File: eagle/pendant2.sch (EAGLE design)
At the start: 7 parts, among them U1 ATTINY85-20PU

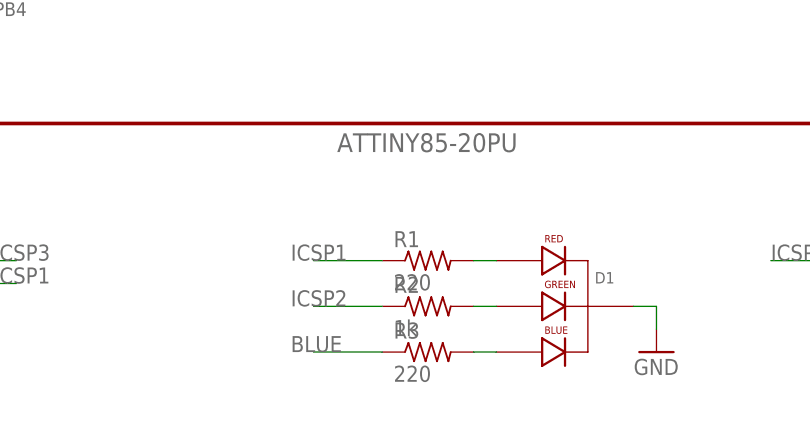
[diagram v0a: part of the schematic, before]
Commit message: Made the board yet smaller
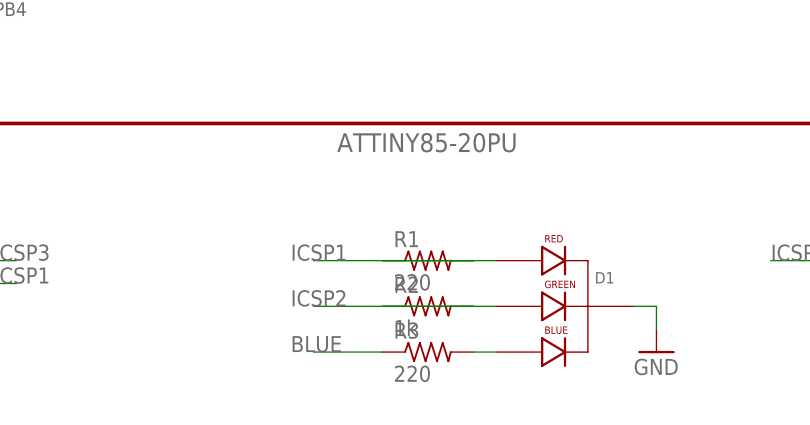
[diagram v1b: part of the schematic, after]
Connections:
- net ICSP1: now also R1.2; no longer R1.1
- net ICSP2: now also R2.2; no longer R2.1
- net N$1: now also R1.1; no longer R1.2
- net N$2: now also R2.1; no longer R2.2
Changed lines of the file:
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@@
 <net name="N$1" class="0">
 <segment>
-<pinref part="R1" gate="G$1" pin="2"/>
+<pinref part="R1" gate="G$1" pin="1"/>
 <pinref part="D1" gate="G$1" pin="RED_CATHODE"/>
-<wire x1="88.9" y1="17.78" x2="91.44" y2="17.78" width="0.1524" layer="91"/>
+<wire x1="78.74" y1="17.78" x2="91.44" y2="17.78" width="0.1524" layer="91"/>
 </segment>
 </net>
 <net name="N$2" class="0">
 <segment>
-<pinref part="R2" gate="G$1" pin="2"/>
+<pinref part="R2" gate="G$1" pin="1"/>
 <pinref part="D1" gate="G$1" pin="GREEN_CATHODE"/>
-<wire x1="88.9" y1="12.7" x2="91.44" y2="12.7" width="0.1524" layer="91"/>
+<wire x1="78.74" y1="12.7" x2="91.44" y2="12.7" width="0.1524" layer="91"/>
 </segment>
 </net>
@@
 </segment>
 <segment>
-<pinref part="R1" gate="G$1" pin="1"/>
-<wire x1="78.74" y1="17.78" x2="71.12" y2="17.78" width="0.1524" layer="91"/>
+<pinref part="R1" gate="G$1" pin="2"/>
+<wire x1="88.9" y1="17.78" x2="71.12" y2="17.78" width="0.1524" layer="91"/>
 <label x="68.58" y="17.78" size="1.778" layer="95"/>
 </segment>
@@
 </segment>
 <segment>
-<pinref part="R2" gate="G$1" pin="1"/>
-<wire x1="78.74" y1="12.7" x2="71.12" y2="12.7" width="0.1524" layer="91"/>
+<pinref part="R2" gate="G$1" pin="2"/>
+<wire x1="88.9" y1="12.7" x2="71.12" y2="12.7" width="0.1524" layer="91"/>
 <label x="68.58" y="12.7" size="1.778" layer="95"/>
 </segment>

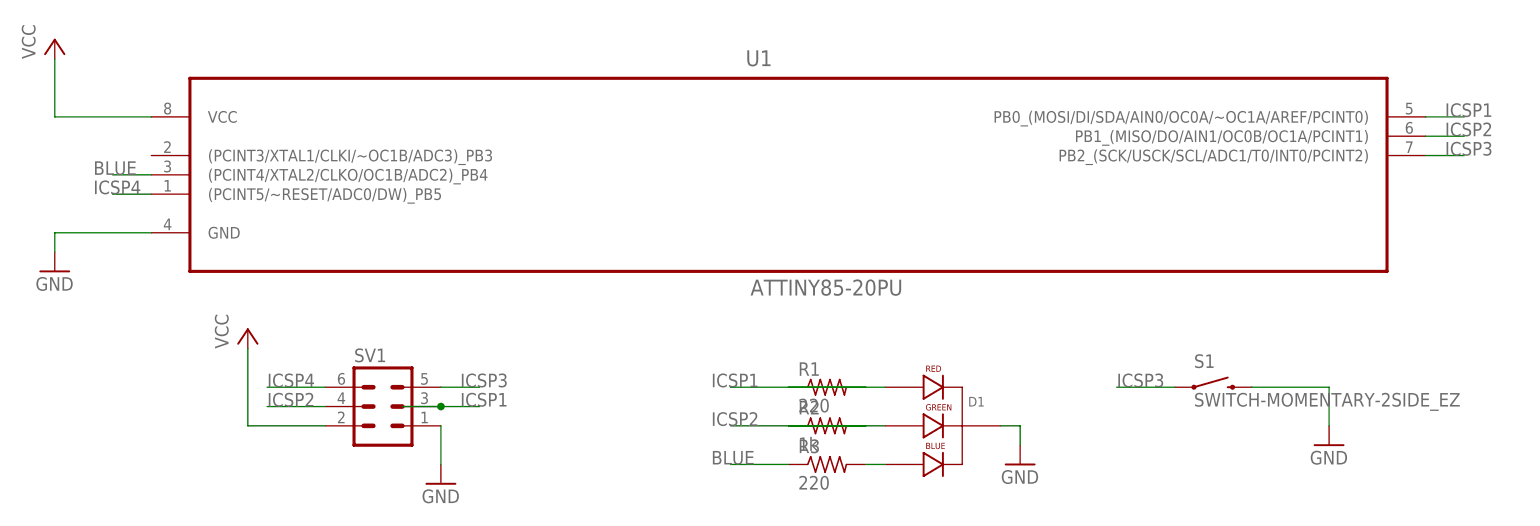
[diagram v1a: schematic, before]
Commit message: replacing ATtiny part with SparkFun version for standardizing
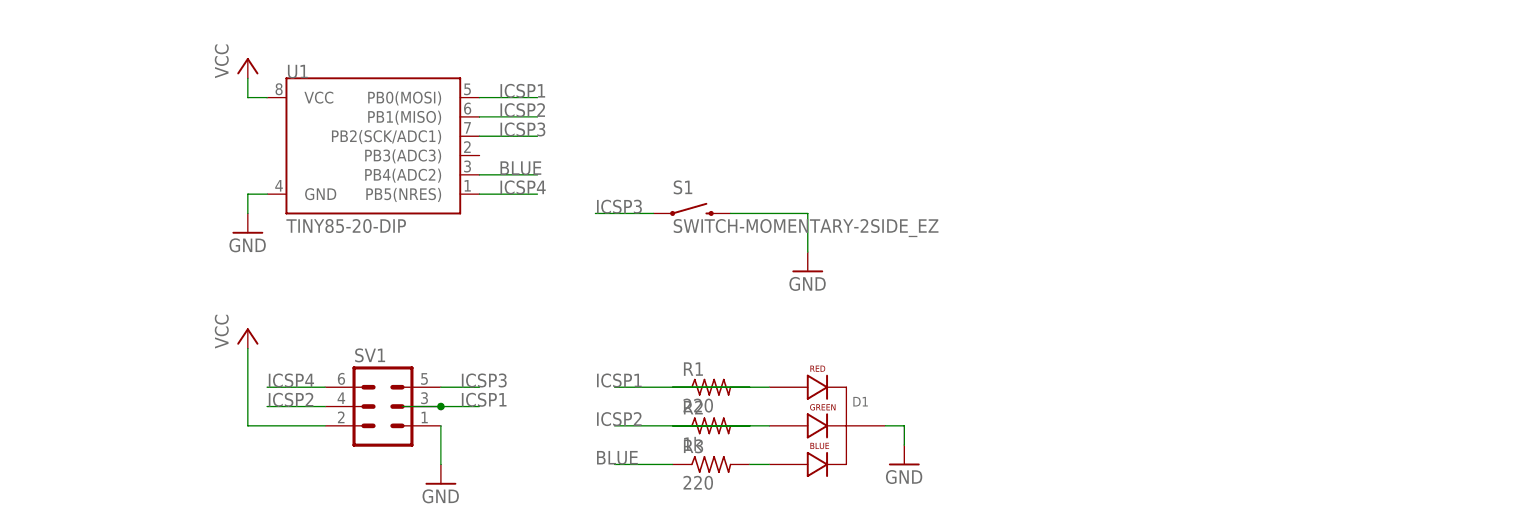
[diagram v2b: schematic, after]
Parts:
- U1: value ATTINY85-20PU -> TINY85-20-DIP; device Atmel_By_element14_Batch_1-00:ATTINY85-20PU -> SparkFun-DigitalIC:ATTINY45TINY85-20-DIP
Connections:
- net BLUE: now also U1.PB4(ADC2); no longer U1.(PCINT4/XTAL2/CLKO/OC1B/ADC2)_PB4
- net ICSP1: now also U1.PB0(MOSI); no longer U1.PB0_(MOSI/DI/SDA/AIN0/OC0A/~OC1A/AREF/PCINT0)
- net ICSP2: now also U1.PB1(MISO); no longer U1.PB1_(MISO/DO/AIN1/OC0B/OC1A/PCINT1)
- net ICSP3: now also U1.PB2(SCK/ADC1); no longer U1.PB2_(SCK/USCK/SCL/ADC1/T0/INT0/PCINT2)
- net ICSP4: now also U1.PB5(NRES); no longer U1.(PCINT5/~RESET/ADC0/DW)_PB5
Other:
- moved on the sheet: D1, R1, R2, R3, S1
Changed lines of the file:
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@@
 </classes>
 <parts>
-<part name="U1" library="Atmel_By_element14_Batch_1-00" deviceset="ATTINY85-20PU" device=""/>
 <part name="GND1" library="supply1" deviceset="GND" device=""/>
 <part name="GND2" library="supply1" deviceset="GND" device=""/>
@@
 <part name="R3" library="rcl" deviceset="R-US_" device="0411/3V" value="220"/>
 <part name="S1" library="SparkFun-Electromechanical" deviceset="SWITCH-MOMENTARY-2" device="SIDE_EZ"/>
+<part name="U1" library="SparkFun-DigitalIC" deviceset="ATTINY45" device="TINY85-20-DIP" value="TINY85-20-DIP"/>
 </parts>
 <sheets>
@@
 </plain>
 <instances>
-<instance part="U1" gate="A" x="78.74" y="48.26"/>
-<instance part="GND1" gate="1" x="-17.78" y="33.02"/>
-<instance part="GND2" gate="1" x="149.86" y="10.16"/>
-<instance part="GND3" gate="1" x="109.22" y="7.62"/>
+<instance part="GND1" gate="1" x="7.62" y="38.1"/>
+<instance part="GND2" gate="1" x="81.28" y="33.02"/>
+<instance part="GND3" gate="1" x="93.98" y="7.62"/>
 <instance part="GND4" gate="1" x="33.02" y="5.08"/>
-<instance part="P+1" gate="VCC" x="-17.78" y="63.5"/>
+<instance part="P+1" gate="VCC" x="7.62" y="60.96"/>
 <instance part="P+2" gate="VCC" x="7.62" y="25.4"/>
-<instance part="D1" gate="G$1" x="96.52" y="12.7"/>
+<instance part="D1" gate="G$1" x="81.28" y="12.7"/>
 <instance part="SV1" gate="1" x="25.4" y="15.24"/>
-<instance part="R1" gate="G$1" x="83.82" y="17.78"/>
-<instance part="R2" gate="G$1" x="83.82" y="12.7"/>
-<instance part="R3" gate="G$1" x="83.82" y="7.62"/>
-<instance part="S1" gate="G$1" x="134.62" y="17.78"/>
+<instance part="R1" gate="G$1" x="68.58" y="17.78"/>
+<instance part="R2" gate="G$1" x="68.58" y="12.7"/>
+<instance part="R3" gate="G$1" x="68.58" y="7.62"/>
+<instance part="S1" gate="G$1" x="66.04" y="40.64"/>
+<instance part="U1" gate="G$1" x="25.4" y="48.26"/>
 </instances>
 <busses>
@@
 <pinref part="R1" gate="G$1" pin="1"/>
 <pinref part="D1" gate="G$1" pin="RED_CATHODE"/>
-<wire x1="78.74" y1="17.78" x2="91.44" y2="17.78" width="0.1524" layer="91"/>
+<wire x1="63.5" y1="17.78" x2="76.2" y2="17.78" width="0.1524" layer="91"/>
 </segment>
 </net>
@@
 <pinref part="R2" gate="G$1" pin="1"/>
 <pinref part="D1" gate="G$1" pin="GREEN_CATHODE"/>
-<wire x1="78.74" y1="12.7" x2="91.44" y2="12.7" width="0.1524" layer="91"/>
+<wire x1="63.5" y1="12.7" x2="76.2" y2="12.7" width="0.1524" layer="91"/>
 </segment>
 </net>
@@
 <pinref part="R3" gate="G$1" pin="2"/>
 <pinref part="D1" gate="G$1" pin="BLUE_CATHODE"/>
-<wire x1="88.9" y1="7.62" x2="91.44" y2="7.62" width="0.1524" layer="91"/>
+<wire x1="73.66" y1="7.62" x2="76.2" y2="7.62" width="0.1524" layer="91"/>
 </segment>
 </net>
 <net name="VCC" class="0">
 <segment>
-<pinref part="U1" gate="A" pin="VCC"/>
-<wire x1="-5.08" y1="53.34" x2="-17.78" y2="53.34" width="0.1524" layer="91"/>
 <pinref part="P+1" gate="VCC" pin="VCC"/>
-<wire x1="-17.78" y1="53.34" x2="-17.78" y2="60.96" width="0.1524" layer="91"/>
+<wire x1="7.62" y1="55.88" x2="7.62" y2="58.42" width="0.1524" layer="91"/>
+<pinref part="U1" gate="G$1" pin="VCC"/>
+<wire x1="7.62" y1="55.88" x2="10.16" y2="55.88" width="0.1524" layer="91"/>
 </segment>
 <segment>
@@
 <net name="GND" class="0">
 <segment>
-<pinref part="U1" gate="A" pin="GND"/>
-<wire x1="-5.08" y1="38.1" x2="-17.78" y2="38.1" width="0.1524" layer="91"/>
 <pinref part="GND1" gate="1" pin="GND"/>
-<wire x1="-17.78" y1="38.1" x2="-17.78" y2="35.56" width="0.1524" layer="91"/>
+<wire x1="7.62" y1="40.64" x2="7.62" y2="43.18" width="0.1524" layer="91"/>
+<pinref part="U1" gate="G$1" pin="GND"/>
+<wire x1="7.62" y1="43.18" x2="10.16" y2="43.18" width="0.1524" layer="91"/>
 </segment>
 <segment>
 <pinref part="D1" gate="G$1" pin="CATHODE"/>
-<wire x1="106.68" y1="12.7" x2="109.22" y2="12.7" width="0.1524" layer="91"/>
+<wire x1="91.44" y1="12.7" x2="93.98" y2="12.7" width="0.1524" layer="91"/>
 <pinref part="GND3" gate="1" pin="GND"/>
-<wire x1="109.22" y1="12.7" x2="109.22" y2="10.16" width="0.1524" layer="91"/>
+<wire x1="93.98" y1="12.7" x2="93.98" y2="10.16" width="0.1524" layer="91"/>
 </segment>
 <segment>
@@
 <segment>
 <pinref part="S1" gate="G$1" pin="2"/>
-<wire x1="139.7" y1="17.78" x2="149.86" y2="17.78" width="0.1524" layer="91"/>
+<wire x1="71.12" y1="40.64" x2="81.28" y2="40.64" width="0.1524" layer="91"/>
 <pinref part="GND2" gate="1" pin="GND"/>
-<wire x1="149.86" y1="17.78" x2="149.86" y2="12.7" width="0.1524" layer="91"/>
+<wire x1="81.28" y1="40.64" x2="81.28" y2="35.56" width="0.1524" layer="91"/>
 </segment>
 </net>
 <net name="ICSP1" class="0">
-<segment>
-<pinref part="U1" gate="A" pin="PB0_(MOSI/DI/SDA/AIN0/OC0A/~OC1A/AREF/PCINT0)"/>
-<wire x1="162.56" y1="53.34" x2="167.64" y2="53.34" width="0.1524" layer="91"/>
-<label x="165.1" y="53.34" size="1.778" layer="95"/>
-</segment>
 <segment>
 <wire x1="27.94" y1="15.24" x2="33.02" y2="15.24" width="0.1524" layer="91"/>
@@
 <segment>
 <pinref part="R1" gate="G$1" pin="2"/>
-<wire x1="88.9" y1="17.78" x2="71.12" y2="17.78" width="0.1524" layer="91"/>
-<label x="68.58" y="17.78" size="1.778" layer="95"/>
+<wire x1="73.66" y1="17.78" x2="55.88" y2="17.78" width="0.1524" layer="91"/>
+<label x="53.34" y="17.78" size="1.778" layer="95"/>
+</segment>
+<segment>
+<pinref part="U1" gate="G$1" pin="PB0(MOSI)"/>
+<wire x1="38.1" y1="55.88" x2="45.72" y2="55.88" width="0.1524" layer="91"/>
+<label x="40.64" y="55.88" size="1.778" layer="95"/>
 </segment>
 </net>
 <net name="ICSP2" class="0">
-<segment>
-<pinref part="U1" gate="A" pin="PB1_(MISO/DO/AIN1/OC0B/OC1A/PCINT1)"/>
-<wire x1="162.56" y1="50.8" x2="167.64" y2="50.8" width="0.1524" layer="91"/>
-<label x="165.1" y="50.8" size="1.778" layer="95"/>
-</segment>
 <segment>
 <pinref part="SV1" gate="1" pin="4"/>
@@
 <segment>
 <pinref part="R2" gate="G$1" pin="2"/>
-<wire x1="88.9" y1="12.7" x2="71.12" y2="12.7" width="0.1524" layer="91"/>
-<label x="68.58" y="12.7" size="1.778" layer="95"/>
+<wire x1="73.66" y1="12.7" x2="55.88" y2="12.7" width="0.1524" layer="91"/>
+<label x="53.34" y="12.7" size="1.778" layer="95"/>
+</segment>
+<segment>
+<pinref part="U1" gate="G$1" pin="PB1(MISO)"/>
+<wire x1="38.1" y1="53.34" x2="45.72" y2="53.34" width="0.1524" layer="91"/>
+<label x="40.64" y="53.34" size="1.778" layer="95"/>
 </segment>
 </net>
 <net name="ICSP3" class="0">
-<segment>
-<pinref part="U1" gate="A" pin="PB2_(SCK/USCK/SCL/ADC1/T0/INT0/PCINT2)"/>
-<wire x1="162.56" y1="48.26" x2="167.64" y2="48.26" width="0.1524" layer="91"/>
-<label x="165.1" y="48.26" size="1.778" layer="95"/>
-</segment>
 <segment>
 <pinref part="SV1" gate="1" pin="5"/>
@@
 <segment>
 <pinref part="S1" gate="G$1" pin="1"/>
-<wire x1="129.54" y1="17.78" x2="121.92" y2="17.78" width="0.1524" layer="91"/>
-<label x="121.92" y="17.78" size="1.778" layer="95"/>
+<wire x1="60.96" y1="40.64" x2="53.34" y2="40.64" width="0.1524" layer="91"/>
+<label x="53.34" y="40.64" size="1.778" layer="95"/>
+</segment>
+<segment>
+<pinref part="U1" gate="G$1" pin="PB2(SCK/ADC1)"/>
+<wire x1="38.1" y1="50.8" x2="45.72" y2="50.8" width="0.1524" layer="91"/>
+<label x="40.64" y="50.8" size="1.778" layer="95"/>
 </segment>
 </net>
 <net name="ICSP4" class="0">
-<segment>
-<pinref part="U1" gate="A" pin="(PCINT5/~RESET/ADC0/DW)_PB5"/>
-<wire x1="-5.08" y1="43.18" x2="-10.16" y2="43.18" width="0.1524" layer="91"/>
-<label x="-12.7" y="43.18" size="1.778" layer="95"/>
-</segment>
 <segment>
 <pinref part="SV1" gate="1" pin="6"/>
@@
 <label x="10.16" y="17.78" size="1.778" layer="95"/>
 </segment>
+<segment>
+<pinref part="U1" gate="G$1" pin="PB5(NRES)"/>
+<wire x1="38.1" y1="43.18" x2="45.72" y2="43.18" width="0.1524" layer="91"/>
+<label x="40.64" y="43.18" size="1.778" layer="95"/>
+</segment>
 </net>
 <net name="BLUE" class="0">
 <segment>
-<pinref part="U1" gate="A" pin="(PCINT4/XTAL2/CLKO/OC1B/ADC2)_PB4"/>
-<wire x1="-5.08" y1="45.72" x2="-10.16" y2="45.72" width="0.1524" layer="91"/>
-<label x="-12.7" y="45.72" size="1.778" layer="95"/>
+<pinref part="R3" gate="G$1" pin="1"/>
+<wire x1="63.5" y1="7.62" x2="55.88" y2="7.62" width="0.1524" layer="91"/>
+<label x="53.34" y="7.62" size="1.778" layer="95"/>
 </segment>
 <segment>
-<pinref part="R3" gate="G$1" pin="1"/>
-<wire x1="78.74" y1="7.62" x2="71.12" y2="7.62" width="0.1524" layer="91"/>
-<label x="68.58" y="7.62" size="1.778" layer="95"/>
+<pinref part="U1" gate="G$1" pin="PB4(ADC2)"/>
+<wire x1="38.1" y1="45.72" x2="45.72" y2="45.72" width="0.1524" layer="91"/>
+<label x="40.64" y="45.72" size="1.778" layer="95"/>
 </segment>
 </net>
